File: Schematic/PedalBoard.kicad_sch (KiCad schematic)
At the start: 18 parts, among them U1 SC0918, U2 ADS1115IDGST, U3 ADS1115IDGST, U4 THB001P

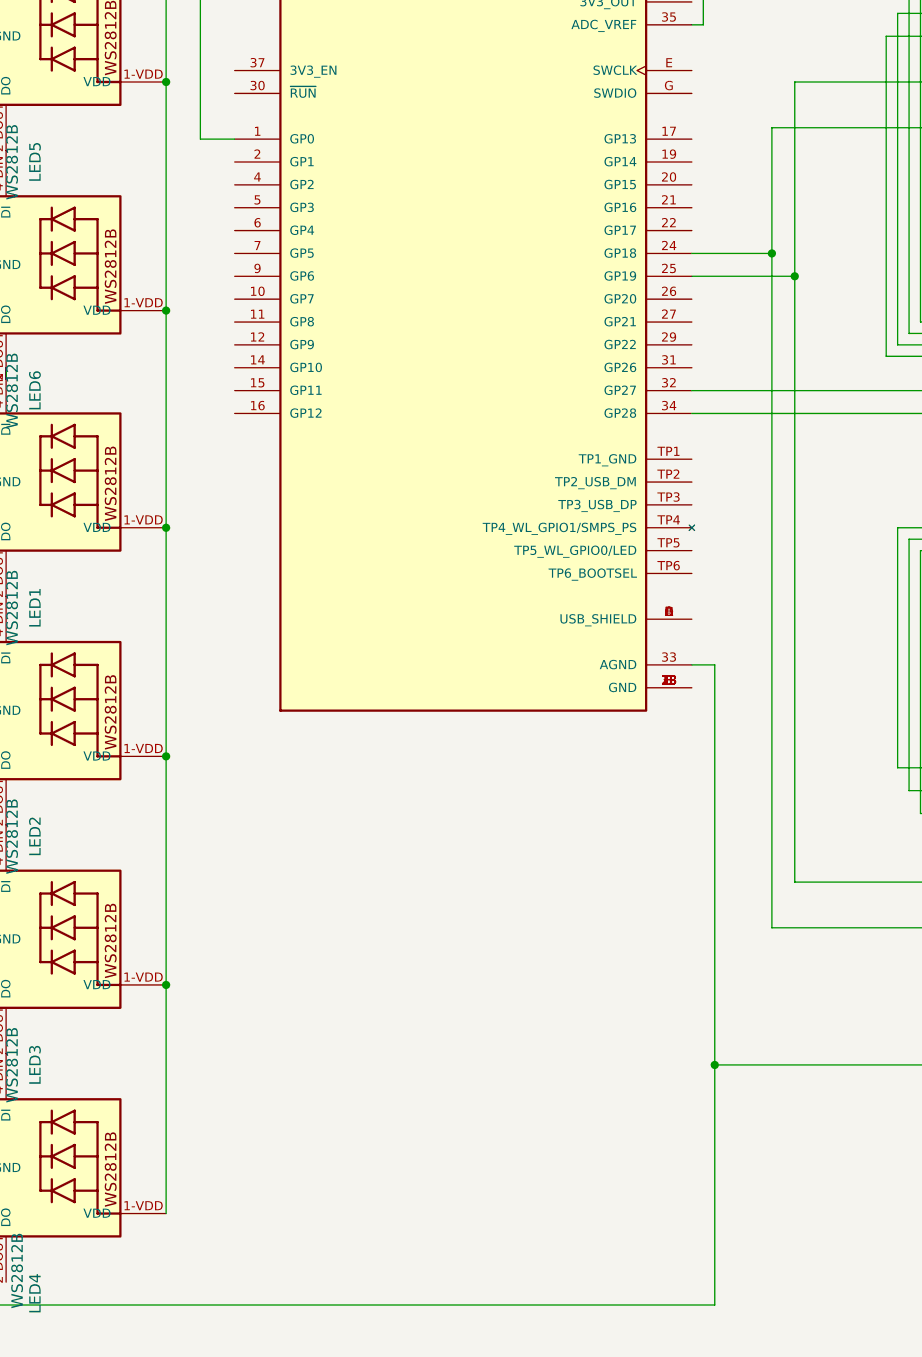
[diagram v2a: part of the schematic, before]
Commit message: Added mx switches to schematic
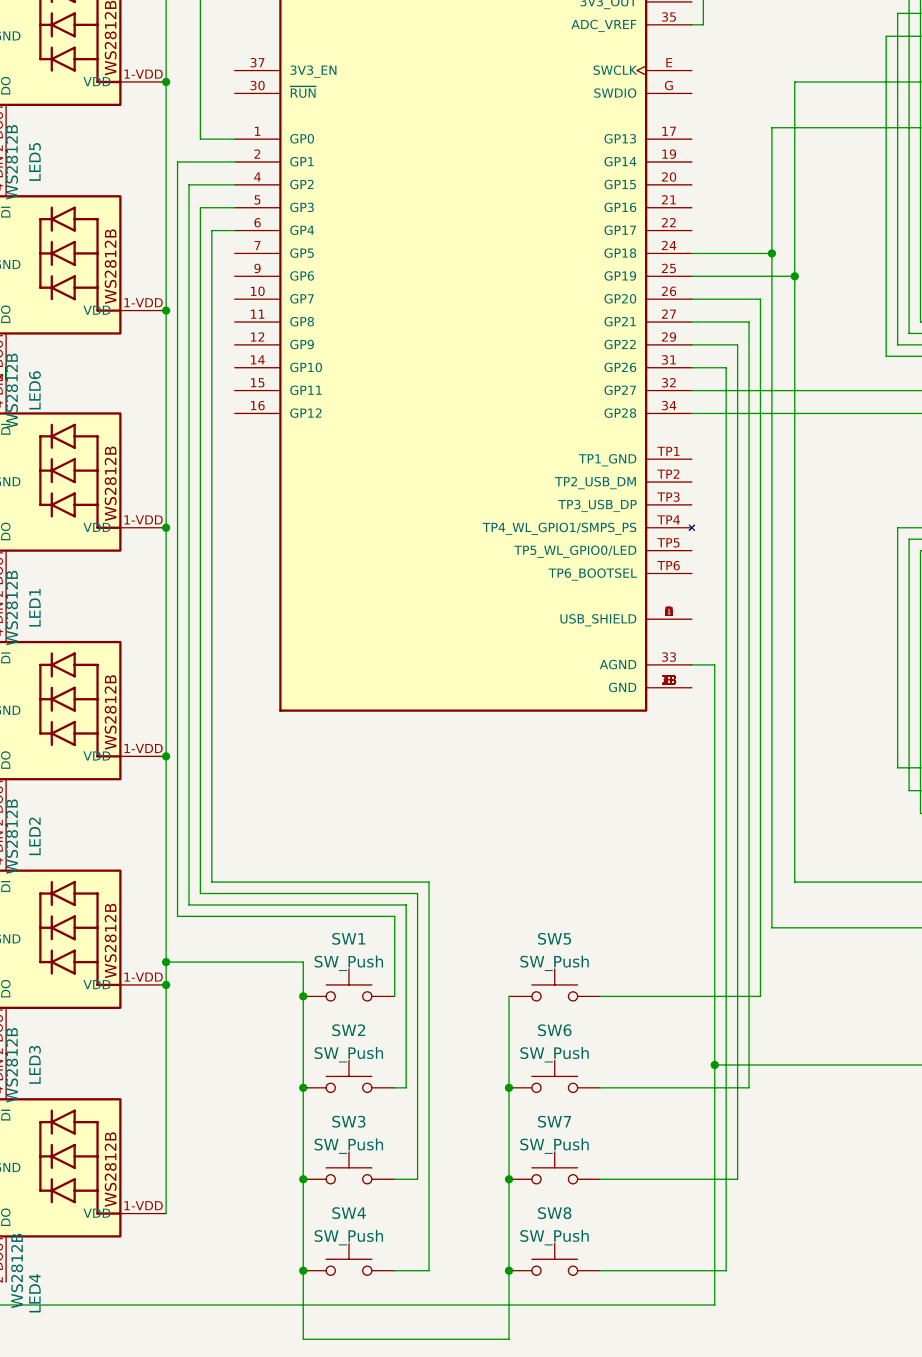
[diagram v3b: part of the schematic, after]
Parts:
- added SW1, SW2, SW3, SW4, SW5, SW6, SW7, SW8: SW_Push, symbol Switch:SW_Push
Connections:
- net at LED1.1-VDD (VDD), LED2.1-VDD (VDD), LED3.1-VDD (VDD)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: now also SW1.1, SW2.1, SW3.1, SW4.1, SW5.1, SW6.1, SW7.1, SW8.1
- net at U1.2 (GP1): now also SW1.2
- net at U1.26 (GP20): now also SW5.2
- net at U1.27 (GP21): now also SW6.2
- net at U1.29 (GP22): now also SW7.2
- net at U1.31 (GP26): now also SW8.2
- net at U1.4 (GP2): now also SW2.2
- net at U1.5 (GP3): now also SW3.2
- net at U1.6 (GP4): now also SW4.2

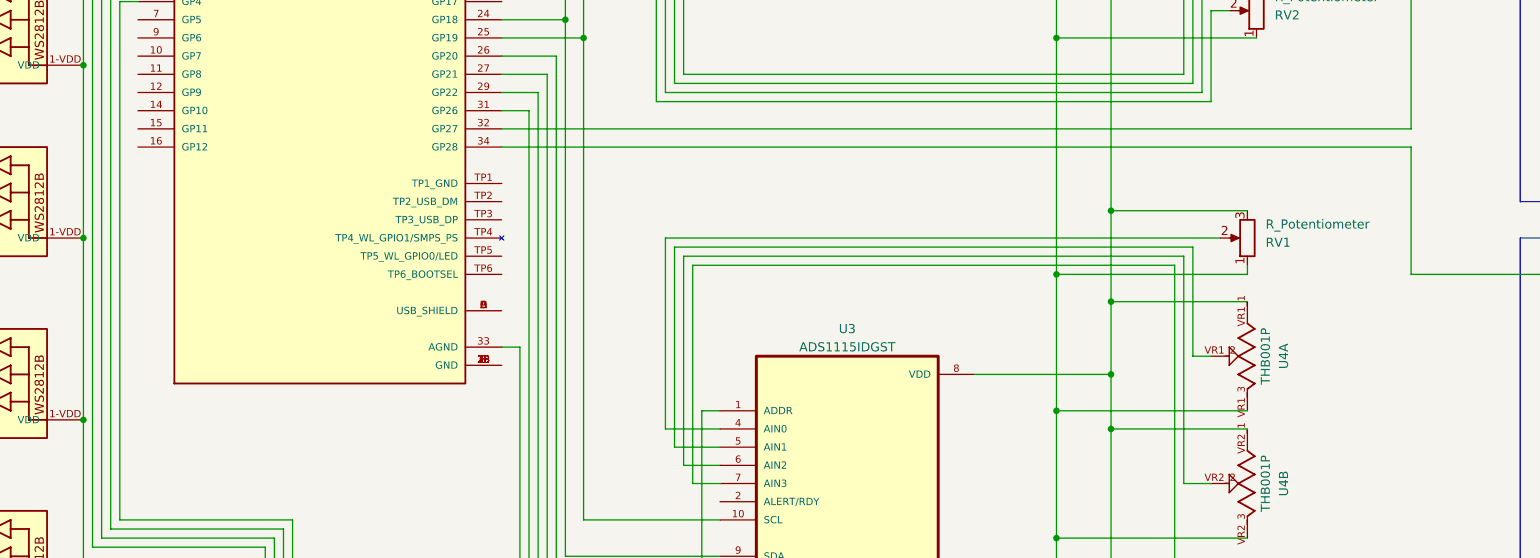
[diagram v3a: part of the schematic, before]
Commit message: Added Stomp buttons,corrected schematic
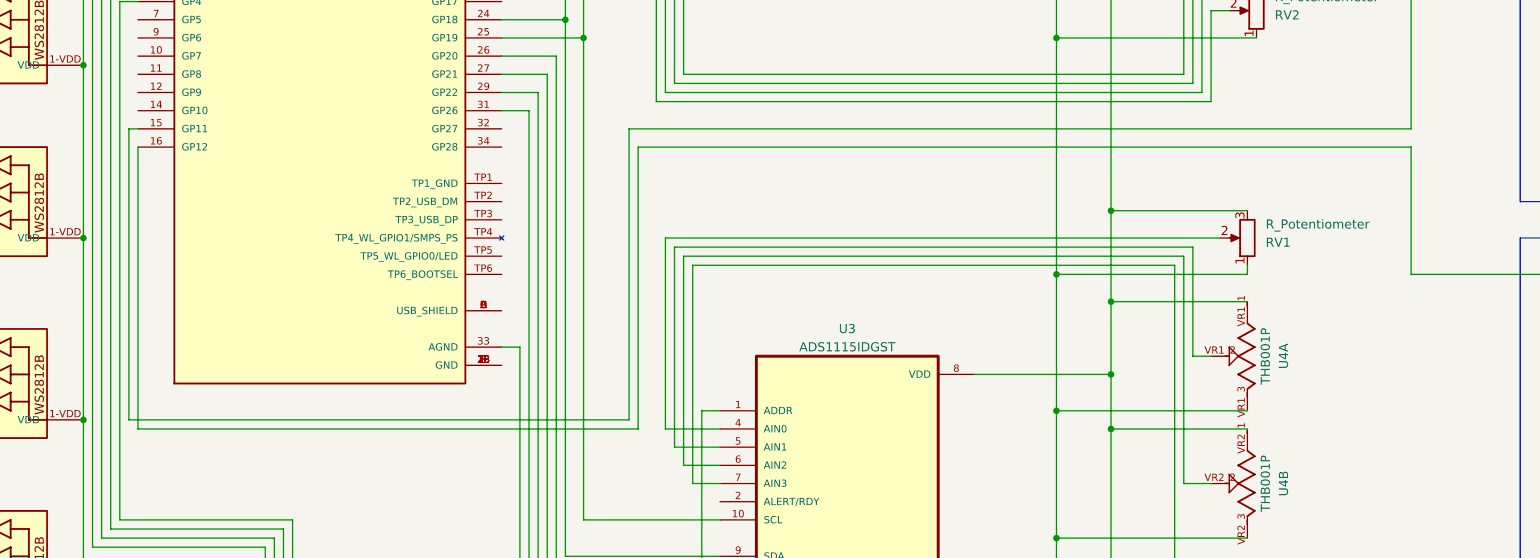
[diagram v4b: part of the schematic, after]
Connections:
- net at S2.P$9 (S): now also U1.16 (GP12); no longer U1.34 (GP28)
- net at S1.P$9 (S): now also U1.15 (GP11); no longer U1.32 (GP27)
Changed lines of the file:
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@@
+    (stroke (width 0) (type default))
+  )
+  (wire (pts (xy 54.61 88.9) (xy 55.88 88.9))
     (stroke (width 0) (type default))
   )
@@
     (stroke (width 0) (type default))
   )
-  (wire (pts (xy 233.68 91.44) (xy 106.68 91.44))
-    (stroke (width 0) (type default))
-  )
   (wire (pts (xy 200.66 107.95) (xy 200.66 154.94))
     (stroke (width 0) (type default))
@@
     (stroke (width 0) (type default))
   )
+  (wire (pts (xy 124.46 88.9) (xy 124.46 129.54))
+    (stroke (width 0) (type default))
+  )
   (wire (pts (xy 132.08 135.89) (xy 137.16 135.89))
     (stroke (width 0) (type default))
@@
     (stroke (width 0) (type default))
   )
+  (wire (pts (xy 124.46 129.54) (xy 54.61 129.54))
+    (stroke (width 0) (type default))
+  )
   (wire (pts (xy 63.5 166.37) (xy 63.5 176.53))
     (stroke (width 0) (type default))
@@
     (stroke (width 0) (type default))
   )
+  (wire (pts (xy 125.73 130.81) (xy 125.73 91.44))
+    (stroke (width 0) (type default))
+  )
   (wire (pts (xy 191.77 45.72) (xy 191.77 34.29))
     (stroke (width 0) (type default))
@@
     (stroke (width 0) (type default))
   )
-  (wire (pts (xy 233.68 88.9) (xy 106.68 88.9))
-    (stroke (width 0) (type default))
-  )
   (wire (pts (xy 233.68 109.22) (xy 233.68 91.44))
     (stroke (width 0) (type default))
@@
     (stroke (width 0) (type default))
   )
+  (wire (pts (xy 233.68 88.9) (xy 124.46 88.9))
+    (stroke (width 0) (type default))
+  )
   (wire (pts (xy 191.77 130.81) (xy 210.82 130.81))
     (stroke (width 0) (type default))
@@
     (stroke (width 0) (type default))
   )
+  (wire (pts (xy 54.61 129.54) (xy 54.61 88.9))
+    (stroke (width 0) (type default))
+  )
   (wire (pts (xy 129.54 104.14) (xy 129.54 130.81))
     (stroke (width 0) (type default))
@@
     (stroke (width 0) (type default))
   )
+  (wire (pts (xy 125.73 91.44) (xy 233.68 91.44))
+    (stroke (width 0) (type default))
+  )
   (wire (pts (xy 110.49 186.69) (xy 96.52 186.69))
     (stroke (width 0) (type default))
@@
     (stroke (width 0) (type default))
   )
+  (wire (pts (xy 55.88 130.81) (xy 125.73 130.81))
+    (stroke (width 0) (type default))
+  )
   (wire (pts (xy 184.15 64.77) (xy 184.15 53.34))
     (stroke (width 0) (type default))
@@
     (stroke (width 0) (type default))
   )
+  (wire (pts (xy 55.88 91.44) (xy 55.88 130.81))
+    (stroke (width 0) (type default))
+  )

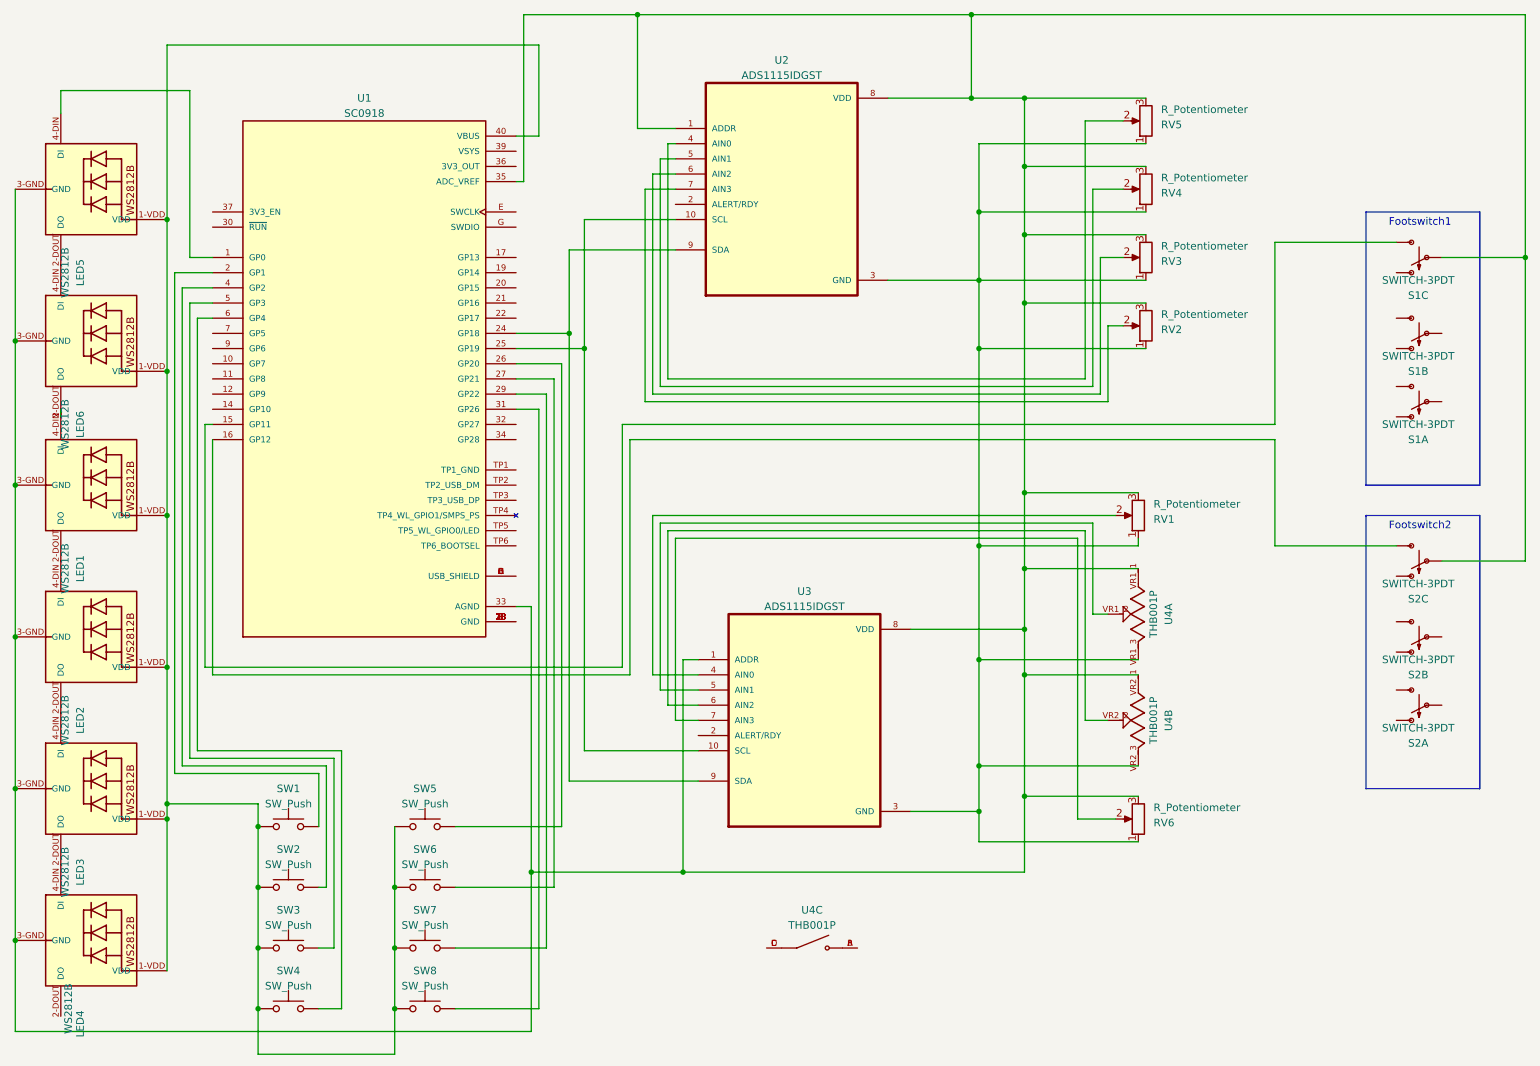
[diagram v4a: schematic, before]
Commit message: added model files for the smaller pedal + fixed kicad for reduced scope
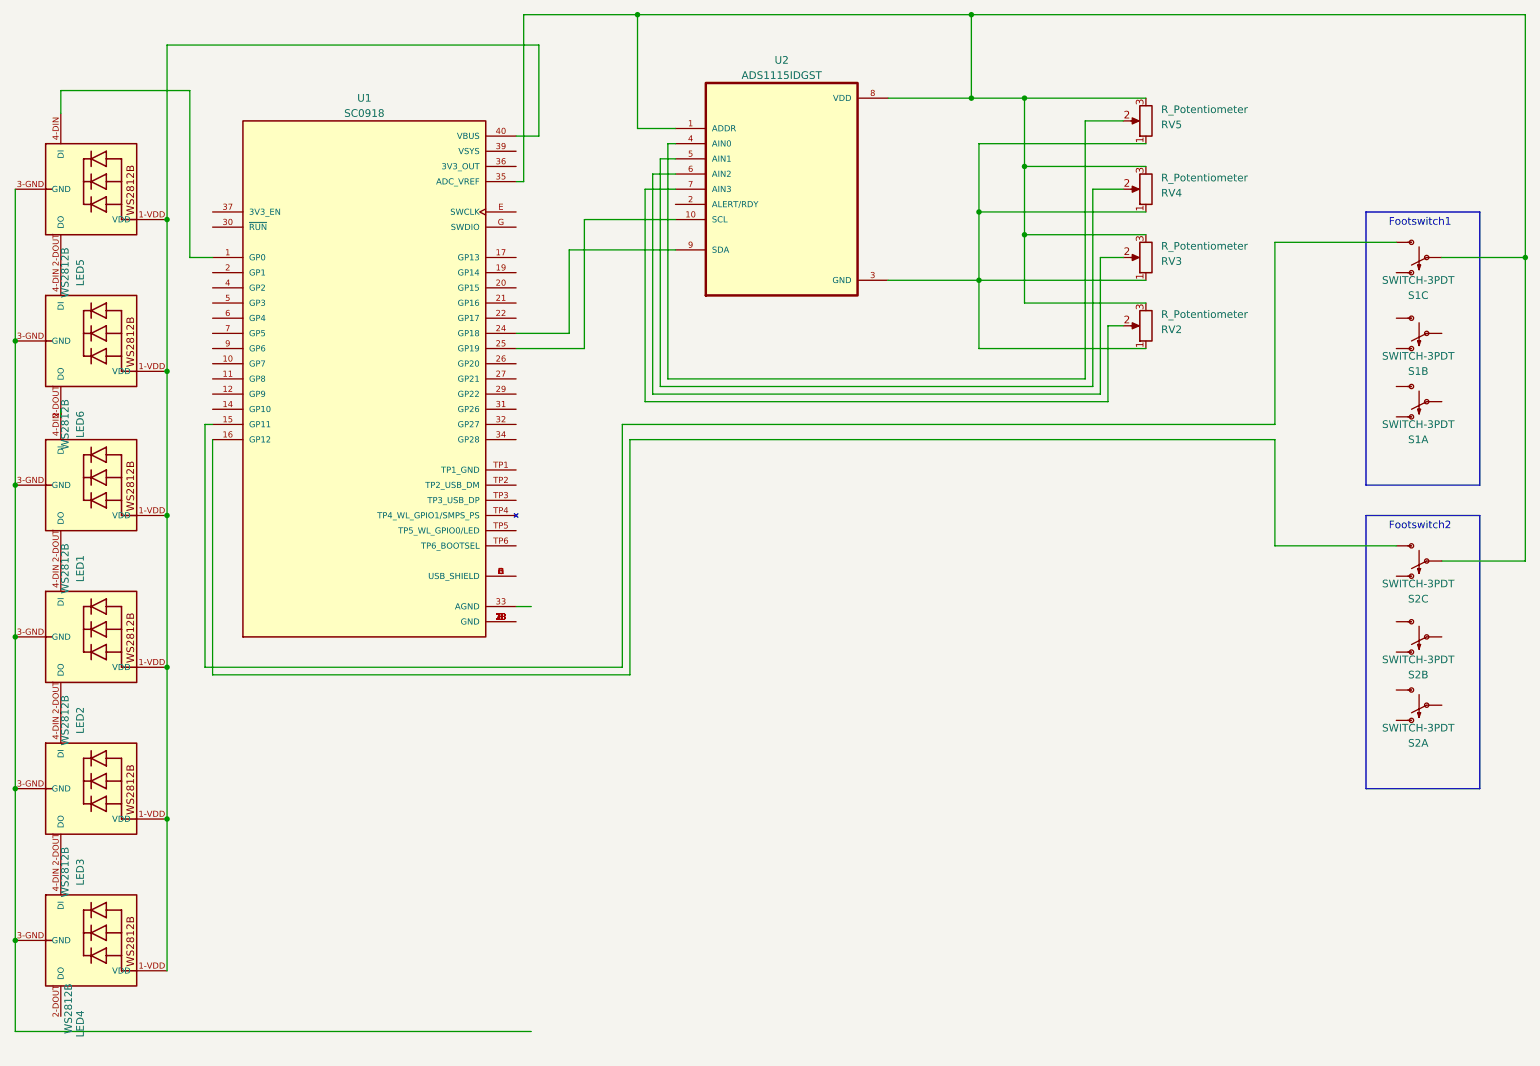
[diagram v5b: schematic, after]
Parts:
- removed RV1, RV6: R_Potentiometer, symbol Device:R_Potentiometer
- removed SW1, SW2, SW3, SW4, SW5, SW6, SW7, SW8: SW_Push, symbol Switch:SW_Push
- removed U3: ADS1115IDGST, SOP50P490X110-10N, symbol ADS1115IDGST:ADS1115IDGST
- removed U4: THB001P, CNK_THB001P, symbol THB001P:THB001P
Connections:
- net at RV2.3, RV3.3, RV4.3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: no longer LED1.3-GND (GND), LED2.3-GND (GND), LED3.3-GND (GND), LED4.3-GND (GND), LED5.3-GND (GND), LED6.3-GND (GND), U1.33 (AGND)
- new net: LED1.3-GND (GND), LED2.3-GND (GND), LED3.3-GND (GND), LED4.3-GND (GND), LED5.3-GND (GND), LED6.3-GND (GND)
